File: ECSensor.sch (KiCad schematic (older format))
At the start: 4 parts

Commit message: Mostly complete Schematic
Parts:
- added Q?: Q_PMOS_DSG, symbol Device:Q_PMOS_DSG
- added R?: 150k, symbol Device:R_Small_US
- added R? (x2): 0, symbol Device:R_Small_US
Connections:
- net RE: now also R?.2
- net WE: now also R?.2
- new net: Q?.1 (D), R?.1
- new net: Q?.2 (S), R?.1
- new net: Q?.3 (G), R?.1
- new net AVDD: R?.2
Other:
- note added: "P-Channel FET used \nto short RE and WE\non power off"
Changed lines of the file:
@@
 $Descr A4 11693 8268
 encoding utf-8
-Sheet 2 2
+Sheet 3 3
 Title ""
 Date ""
@@
 U 1 1 5DF76279
 P 3350 3850
+AR Path="/5DF7340A/5DF76279" Ref="C?"  Part="1"
+AR Path="/5DF54D0C/5DF76279" Ref="C?"  Part="1"
 F 0 "C?" H 3442 3896 50  0000 L CNN
 F 1 "0.1u" H 3442 3805 50  0000 L CNN
@@
 U 1 1 5DF76497
 P 3000 3600
+AR Path="/5DF7340A/5DF76497" Ref="C?"  Part="1"
+AR Path="/5DF54D0C/5DF76497" Ref="C?"  Part="1"
 F 0 "C?" H 3092 3646 50  0000 L CNN
 F 1 "0.1u" H 3092 3555 50  0000 L CNN
@@
 U 1 1 5DF768A0
 P 3700 4100
+AR Path="/5DF7340A/5DF768A0" Ref="C?"  Part="1"
+AR Path="/5DF54D0C/5DF768A0" Ref="C?"  Part="1"
 F 0 "C?" H 3792 4146 50  0000 L CNN
 F 1 "0.1u" H 3792 4055 50  0000 L CNN
@@
 U 1 1 5DF7EEA4
 P 4100 3600
+AR Path="/5DF7340A/5DF7EEA4" Ref="J?"  Part="1"
+AR Path="/5DF54D0C/5DF7EEA4" Ref="J?"  Part="1"
 F 0 "J?" H 3974 3633 50  0000 R CNN
 F 1 "EC_Sensor_Input_3_Pin" H 3974 3542 50  0000 R CNN
@@
 Wire Wire Line
 	3450 3200 3450 3500
+$Comp
+L Device:Q_PMOS_DSG Q?
+U 1 1 5E0080C3
+P 1550 1350
+AR Path="/5DF54D0C/5E0080C3" Ref="Q?"  Part="1"
+AR Path="/5DF7340A/5E0080C3" Ref="Q?"  Part="1"
+F 0 "Q?" H 1755 1396 50  0000 L CNN
+F 1 "Q_PMOS_DSG" H 1755 1305 50  0000 L CNN
+F 2 "" H 1750 1450 50  0001 C CNN
+F 3 "~" H 1550 1350 50  0001 C CNN
+	1    1550 1350
+	1    0    0    -1
+$EndComp
+$Comp
+L Device:R_Small_US R?
+U 1 1 5E00BDC0
+P 1250 1350
+AR Path="/5DF54D0C/5E00BDC0" Ref="R?"  Part="1"
+AR Path="/5DF7340A/5E00BDC0" Ref="R?"  Part="1"
+F 0 "R?" V 1045 1350 50  0000 C CNN
+F 1 "150k" V 1136 1350 50  0000 C CNN
+F 2 "" H 1250 1350 50  0001 C CNN
+F 3 "~" H 1250 1350 50  0001 C CNN
+	1    1250 1350
+	0    1    1    0
+$EndComp
+$Comp
+L Device:R_Small_US R?
+U 1 1 5E00C4B8
+P 1650 1050
+AR Path="/5DF54D0C/5E00C4B8" Ref="R?"  Part="1"
+AR Path="/5DF7340A/5E00C4B8" Ref="R?"  Part="1"
+F 0 "R?" H 1582 1004 50  0000 R CNN
+F 1 "0" H 1582 1095 50  0000 R CNN
+F 2 "" H 1650 1050 50  0001 C CNN
+F 3 "~" H 1650 1050 50  0001 C CNN
+	1    1650 1050
+	-1   0    0    1
+$EndComp
+$Comp
+L Device:R_Small_US R?
+U 1 1 5E00C73E
+P 1650 1650
+AR Path="/5DF54D0C/5E00C73E" Ref="R?"  Part="1"
+AR Path="/5DF7340A/5E00C73E" Ref="R?"  Part="1"
+F 0 "R?" H 1718 1696 50  0000 L CNN
+F 1 "0" H 1718 1605 50  0000 L CNN
+F 2 "" H 1650 1650 50  0001 C CNN
+F 3 "~" H 1650 1650 50  0001 C CNN
+	1    1650 1650
+	1    0    0    -1
+$EndComp
+Text GLabel 1000 1350 0    50   Input ~ 0
+AVDD
+Wire Wire Line
+	1000 1350 1150 1350
+Text Label 3150 2900 2    50   ~ 0
+RE
+Text Label 3150 3050 2    50   ~ 0
+WE
+Text Label 3150 3200 2    50   ~ 0
+CE
+Text Label 1650 800  1    50   ~ 0
+RE
+Text Label 1650 1900 3    50   ~ 0
+WE
+Wire Wire Line
+	1650 1750 1650 1900
+Wire Wire Line
+	1650 950  1650 800
+Wire Notes Line style solid
+	2300 650  2300 2050
+Wire Notes Line style solid
+	2300 2050 700  2050
+Wire Notes Line style solid
+	700  2050 700  650
+Wire Notes Line style solid
+	700  650  2300 650
+Text Notes 750  2000 0    50   ~ 0
+P-Channel FET used \nto short RE and WE\non power off
 $EndSCHEMATC

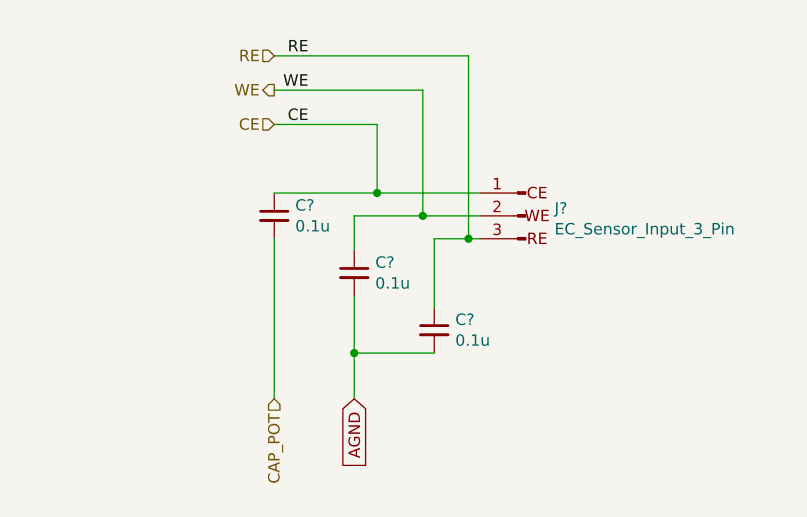
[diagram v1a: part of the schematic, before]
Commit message: Completed Power Supply Filtering
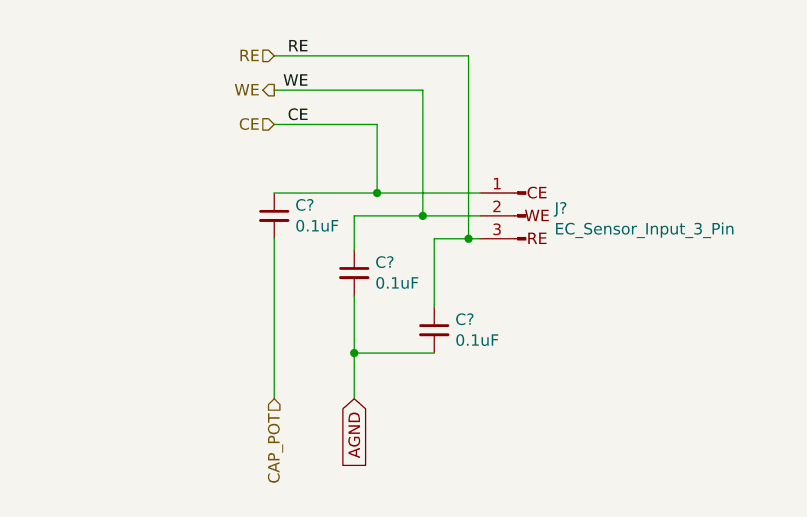
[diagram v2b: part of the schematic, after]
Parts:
- C? (x3): value 0.1u -> 0.1uF
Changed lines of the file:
@@
 AR Path="/5DF54D0C/5DF76279" Ref="C?"  Part="1"
 F 0 "C?" H 3442 3896 50  0000 L CNN
-F 1 "0.1u" H 3442 3805 50  0000 L CNN
+F 1 "0.1uF" H 3442 3805 50  0000 L CNN
 F 2 "" H 3350 3850 50  0001 C CNN
 F 3 "~" H 3350 3850 50  0001 C CNN
@@
 AR Path="/5DF54D0C/5DF76497" Ref="C?"  Part="1"
 F 0 "C?" H 3092 3646 50  0000 L CNN
-F 1 "0.1u" H 3092 3555 50  0000 L CNN
+F 1 "0.1uF" H 3092 3555 50  0000 L CNN
 F 2 "" H 3000 3600 50  0001 C CNN
 F 3 "~" H 3000 3600 50  0001 C CNN
@@
 AR Path="/5DF54D0C/5DF768A0" Ref="C?"  Part="1"
 F 0 "C?" H 3792 4146 50  0000 L CNN
-F 1 "0.1u" H 3792 4055 50  0000 L CNN
+F 1 "0.1uF" H 3792 4055 50  0000 L CNN
 F 2 "" H 3700 4100 50  0001 C CNN
 F 3 "~" H 3700 4100 50  0001 C CNN

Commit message: Working on power input
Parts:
- C37, C38, C39: renamed from C?; footprint (none) -> Capacitor_SMD:C_0603_1608Metric
- J4: renamed from J?; footprint (none) -> Connector_PinHeader_2.54mm:PinHeader_1x03_P2.54mm_Horizontal
- Q2: renamed from Q?; footprint (none) -> Package_TO_SOT_SMD:SOT-23
- R12, R13, R14: renamed from R?; footprint (none) -> Resistor_SMD:R_0603_1608Metric
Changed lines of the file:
@@
 AGND
 $Comp
-L Device:C_Small C?
+L Device:C_Small C38
 U 1 1 5DF76279
 P 3350 3850
-AR Path="/5DF7340A/5DF76279" Ref="C?"  Part="1"
-AR Path="/5DF54D0C/5DF76279" Ref="C?"  Part="1"
-F 0 "C?" H 3442 3896 50  0000 L CNN
+AR Path="/5DF7340A/5DF76279" Ref="C38"  Part="1"
+AR Path="/5DF54D0C/5DF76279" Ref="C41"  Part="1"
+F 0 "C41" H 3442 3896 50  0000 L CNN
 F 1 "0.1uF" H 3442 3805 50  0000 L CNN
-F 2 "" H 3350 3850 50  0001 C CNN
+F 2 "Capacitor_SMD:C_0603_1608Metric" H 3350 3850 50  0001 C CNN
 F 3 "~" H 3350 3850 50  0001 C CNN
 	1    3350 3850
@@
 $EndComp
 $Comp
-L Device:C_Small C?
+L Device:C_Small C37
 U 1 1 5DF76497
 P 3000 3600
-AR Path="/5DF7340A/5DF76497" Ref="C?"  Part="1"
-AR Path="/5DF54D0C/5DF76497" Ref="C?"  Part="1"
-F 0 "C?" H 3092 3646 50  0000 L CNN
+AR Path="/5DF7340A/5DF76497" Ref="C37"  Part="1"
+AR Path="/5DF54D0C/5DF76497" Ref="C40"  Part="1"
+F 0 "C40" H 3092 3646 50  0000 L CNN
 F 1 "0.1uF" H 3092 3555 50  0000 L CNN
-F 2 "" H 3000 3600 50  0001 C CNN
+F 2 "Capacitor_SMD:C_0603_1608Metric" H 3000 3600 50  0001 C CNN
 F 3 "~" H 3000 3600 50  0001 C CNN
 	1    3000 3600
@@
 $EndComp
 $Comp
-L Device:C_Small C?
+L Device:C_Small C39
 U 1 1 5DF768A0
 P 3700 4100
-AR Path="/5DF7340A/5DF768A0" Ref="C?"  Part="1"
-AR Path="/5DF54D0C/5DF768A0" Ref="C?"  Part="1"
-F 0 "C?" H 3792 4146 50  0000 L CNN
+AR Path="/5DF7340A/5DF768A0" Ref="C39"  Part="1"
+AR Path="/5DF54D0C/5DF768A0" Ref="C42"  Part="1"
+F 0 "C42" H 3792 4146 50  0000 L CNN
 F 1 "0.1uF" H 3792 4055 50  0000 L CNN
-F 2 "" H 3700 4100 50  0001 C CNN
+F 2 "Capacitor_SMD:C_0603_1608Metric" H 3700 4100 50  0001 C CNN
 F 3 "~" H 3700 4100 50  0001 C CNN
 	1    3700 4100
@@
 $EndComp
 $Comp
-L chemcrab:EC_Sensor_Input_3_Pin J?
+L chemcrab:EC_Sensor_Input_3_Pin J4
 U 1 1 5DF7EEA4
 P 4100 3600
-AR Path="/5DF7340A/5DF7EEA4" Ref="J?"  Part="1"
-AR Path="/5DF54D0C/5DF7EEA4" Ref="J?"  Part="1"
-F 0 "J?" H 3974 3633 50  0000 R CNN
+AR Path="/5DF7340A/5DF7EEA4" Ref="J4"  Part="1"
+AR Path="/5DF54D0C/5DF7EEA4" Ref="J5"  Part="1"
+F 0 "J5" H 3974 3633 50  0000 R CNN
 F 1 "EC_Sensor_Input_3_Pin" H 3974 3542 50  0000 R CNN
-F 2 "" H 4100 3600 50  0001 C CNN
+F 2 "Connector_PinHeader_2.54mm:PinHeader_1x03_P2.54mm_Horizontal" H 4100 3600 50  0001 C CNN
 F 3 "~" H 4100 3600 50  0001 C CNN
 	1    4100 3600
@@
 	3450 3200 3450 3500
 $Comp
-L Device:Q_PMOS_DSG Q?
+L Device:Q_PMOS_DSG Q2
 U 1 1 5E0080C3
 P 1550 1350
-AR Path="/5DF54D0C/5E0080C3" Ref="Q?"  Part="1"
-AR Path="/5DF7340A/5E0080C3" Ref="Q?"  Part="1"
-F 0 "Q?" H 1755 1396 50  0000 L CNN
+AR Path="/5DF54D0C/5E0080C3" Ref="Q2"  Part="1"
+AR Path="/5DF7340A/5E0080C3" Ref="Q1"  Part="1"
+F 0 "Q2" H 1755 1396 50  0000 L CNN
 F 1 "Q_PMOS_DSG" H 1755 1305 50  0000 L CNN
-F 2 "" H 1750 1450 50  0001 C CNN
+F 2 "Package_TO_SOT_SMD:SOT-23" H 1750 1450 50  0001 C CNN
 F 3 "~" H 1550 1350 50  0001 C CNN
 	1    1550 1350
@@
 $EndComp
 $Comp
-L Device:R_Small_US R?
+L Device:R_Small_US R12
 U 1 1 5E00BDC0
 P 1250 1350
-AR Path="/5DF54D0C/5E00BDC0" Ref="R?"  Part="1"
-AR Path="/5DF7340A/5E00BDC0" Ref="R?"  Part="1"
-F 0 "R?" V 1045 1350 50  0000 C CNN
+AR Path="/5DF54D0C/5E00BDC0" Ref="R12"  Part="1"
+AR Path="/5DF7340A/5E00BDC0" Ref="R9"  Part="1"
+F 0 "R12" V 1045 1350 50  0000 C CNN
 F 1 "150k" V 1136 1350 50  0000 C CNN
-F 2 "" H 1250 1350 50  0001 C CNN
+F 2 "Resistor_SMD:R_0603_1608Metric" H 1250 1350 50  0001 C CNN
 F 3 "~" H 1250 1350 50  0001 C CNN
 	1    1250 1350
@@
 $EndComp
 $Comp
-L Device:R_Small_US R?
+L Device:R_Small_US R13
 U 1 1 5E00C4B8
 P 1650 1050
-AR Path="/5DF54D0C/5E00C4B8" Ref="R?"  Part="1"
-AR Path="/5DF7340A/5E00C4B8" Ref="R?"  Part="1"
-F 0 "R?" H 1582 1004 50  0000 R CNN
+AR Path="/5DF54D0C/5E00C4B8" Ref="R13"  Part="1"
+AR Path="/5DF7340A/5E00C4B8" Ref="R10"  Part="1"
+F 0 "R13" H 1582 1004 50  0000 R CNN
 F 1 "0" H 1582 1095 50  0000 R CNN
-F 2 "" H 1650 1050 50  0001 C CNN
+F 2 "Resistor_SMD:R_0603_1608Metric" H 1650 1050 50  0001 C CNN
 F 3 "~" H 1650 1050 50  0001 C CNN
 	1    1650 1050
@@
 $EndComp
 $Comp
-L Device:R_Small_US R?
+L Device:R_Small_US R14
 U 1 1 5E00C73E
 P 1650 1650
-AR Path="/5DF54D0C/5E00C73E" Ref="R?"  Part="1"
-AR Path="/5DF7340A/5E00C73E" Ref="R?"  Part="1"
-F 0 "R?" H 1718 1696 50  0000 L CNN
+AR Path="/5DF54D0C/5E00C73E" Ref="R14"  Part="1"
+AR Path="/5DF7340A/5E00C73E" Ref="R11"  Part="1"
+F 0 "R14" H 1718 1696 50  0000 L CNN
 F 1 "0" H 1718 1605 50  0000 L CNN
-F 2 "" H 1650 1650 50  0001 C CNN
+F 2 "Resistor_SMD:R_0603_1608Metric" H 1650 1650 50  0001 C CNN
 F 3 "~" H 1650 1650 50  0001 C CNN
 	1    1650 1650

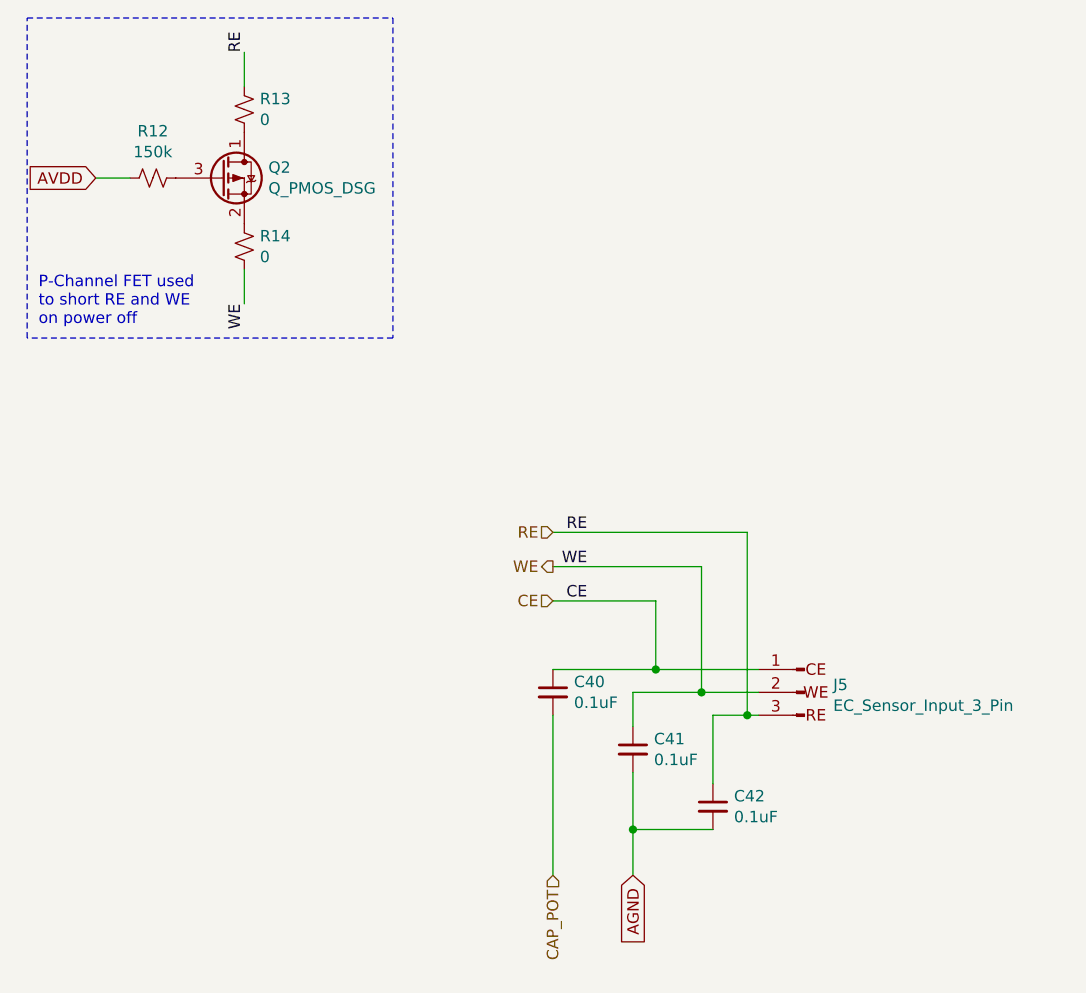
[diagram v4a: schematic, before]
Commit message: Removed unnecessary components
Move things like the Battery Charging circuitry to a separate sheet that can be readded in the future.
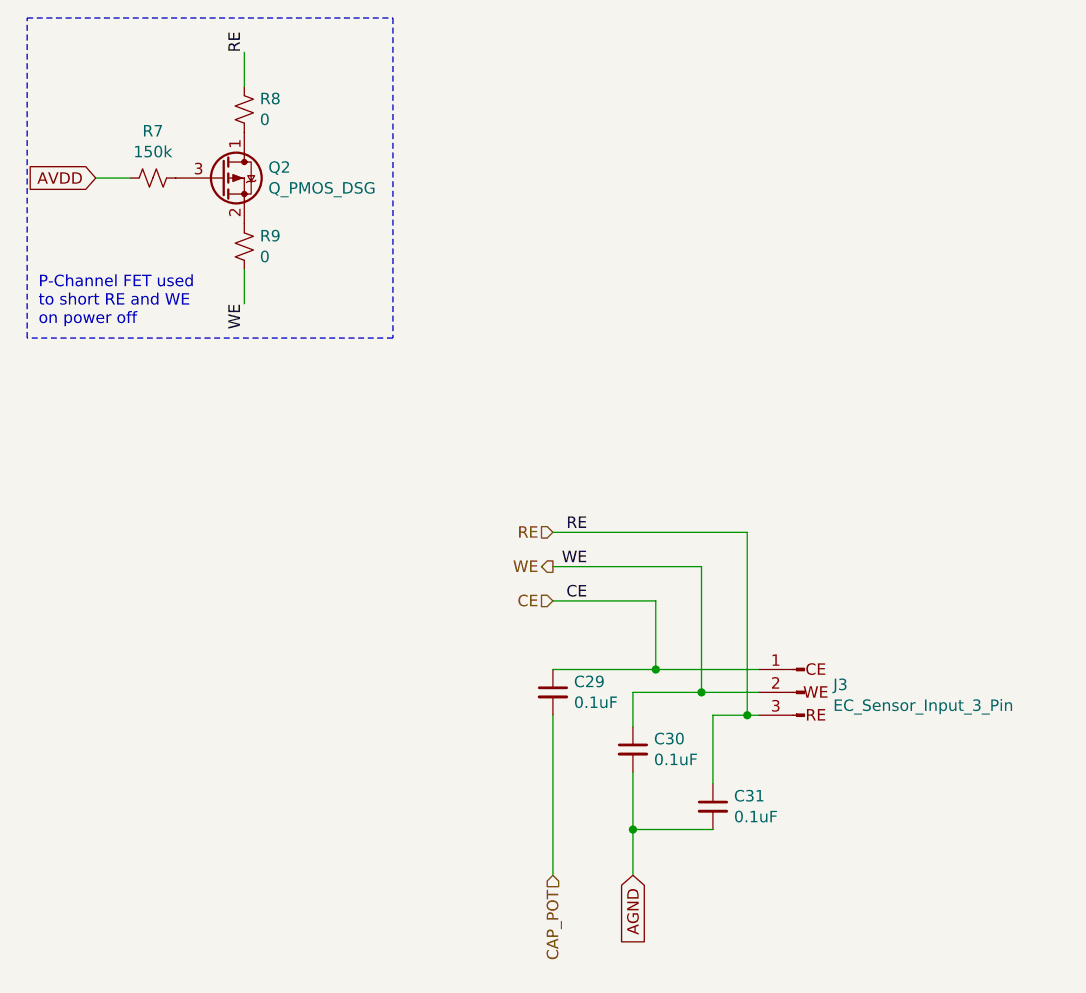
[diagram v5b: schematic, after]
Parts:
- renumbered C37 to C26, C38 to C27, C39 to C28, J4 to J2, R12 to R7, R13 to R8, R14 to R9
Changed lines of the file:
@@
 EESchema Schematic File Version 4
-LIBS:aducm_board-cache
 EELAYER 30 0
 EELAYER END
 $Descr A4 11693 8268
 encoding utf-8
-Sheet 3 4
+Sheet 3 3
 Title "ADuCM355 Template"
 Date ""
@@
 AGND
 $Comp
-L Device:C_Small C38
+L Device:C_Small C27
 U 1 1 5DF76279
 P 3350 3850
-AR Path="/5DF7340A/5DF76279" Ref="C38"  Part="1"
-AR Path="/5DF54D0C/5DF76279" Ref="C41"  Part="1"
-F 0 "C41" H 3442 3896 50  0000 L CNN
+AR Path="/5DF7340A/5DF76279" Ref="C27"  Part="1"
+AR Path="/5DF54D0C/5DF76279" Ref="C30"  Part="1"
+F 0 "C30" H 3442 3896 50  0000 L CNN
 F 1 "0.1uF" H 3442 3805 50  0000 L CNN
 F 2 "Capacitor_SMD:C_0603_1608Metric" H 3350 3850 50  0001 C CNN
@@
 $EndComp
 $Comp
-L Device:C_Small C37
+L Device:C_Small C26
 U 1 1 5DF76497
 P 3000 3600
-AR Path="/5DF7340A/5DF76497" Ref="C37"  Part="1"
-AR Path="/5DF54D0C/5DF76497" Ref="C40"  Part="1"
-F 0 "C40" H 3092 3646 50  0000 L CNN
+AR Path="/5DF7340A/5DF76497" Ref="C26"  Part="1"
+AR Path="/5DF54D0C/5DF76497" Ref="C29"  Part="1"
+F 0 "C29" H 3092 3646 50  0000 L CNN
 F 1 "0.1uF" H 3092 3555 50  0000 L CNN
 F 2 "Capacitor_SMD:C_0603_1608Metric" H 3000 3600 50  0001 C CNN
@@
 $EndComp
 $Comp
-L Device:C_Small C39
+L Device:C_Small C28
 U 1 1 5DF768A0
 P 3700 4100
-AR Path="/5DF7340A/5DF768A0" Ref="C39"  Part="1"
-AR Path="/5DF54D0C/5DF768A0" Ref="C42"  Part="1"
-F 0 "C42" H 3792 4146 50  0000 L CNN
+AR Path="/5DF7340A/5DF768A0" Ref="C28"  Part="1"
+AR Path="/5DF54D0C/5DF768A0" Ref="C31"  Part="1"
+F 0 "C31" H 3792 4146 50  0000 L CNN
 F 1 "0.1uF" H 3792 4055 50  0000 L CNN
 F 2 "Capacitor_SMD:C_0603_1608Metric" H 3700 4100 50  0001 C CNN
@@
 $EndComp
 $Comp
-L chemcrab:EC_Sensor_Input_3_Pin J4
+L chemcrab:EC_Sensor_Input_3_Pin J2
 U 1 1 5DF7EEA4
 P 4100 3600
-AR Path="/5DF7340A/5DF7EEA4" Ref="J4"  Part="1"
-AR Path="/5DF54D0C/5DF7EEA4" Ref="J5"  Part="1"
-F 0 "J5" H 3974 3633 50  0000 R CNN
+AR Path="/5DF7340A/5DF7EEA4" Ref="J2"  Part="1"
+AR Path="/5DF54D0C/5DF7EEA4" Ref="J3"  Part="1"
+F 0 "J3" H 3974 3633 50  0000 R CNN
 F 1 "EC_Sensor_Input_3_Pin" H 3974 3542 50  0000 R CNN
 F 2 "Connector_PinHeader_2.54mm:PinHeader_1x03_P2.54mm_Horizontal" H 4100 3600 50  0001 C CNN
@@
 $EndComp
 $Comp
-L Device:R_Small_US R12
+L Device:R_Small_US R7
 U 1 1 5E00BDC0
 P 1250 1350
-AR Path="/5DF54D0C/5E00BDC0" Ref="R12"  Part="1"
-AR Path="/5DF7340A/5E00BDC0" Ref="R9"  Part="1"
-F 0 "R12" V 1045 1350 50  0000 C CNN
+AR Path="/5DF54D0C/5E00BDC0" Ref="R7"  Part="1"
+AR Path="/5DF7340A/5E00BDC0" Ref="R4"  Part="1"
+F 0 "R7" V 1045 1350 50  0000 C CNN
 F 1 "150k" V 1136 1350 50  0000 C CNN
 F 2 "Resistor_SMD:R_0603_1608Metric" H 1250 1350 50  0001 C CNN
@@
 $EndComp
 $Comp
-L Device:R_Small_US R13
+L Device:R_Small_US R8
 U 1 1 5E00C4B8
 P 1650 1050
-AR Path="/5DF54D0C/5E00C4B8" Ref="R13"  Part="1"
-AR Path="/5DF7340A/5E00C4B8" Ref="R10"  Part="1"
-F 0 "R13" H 1582 1004 50  0000 R CNN
+AR Path="/5DF54D0C/5E00C4B8" Ref="R8"  Part="1"
+AR Path="/5DF7340A/5E00C4B8" Ref="R5"  Part="1"
+F 0 "R8" H 1582 1004 50  0000 R CNN
 F 1 "0" H 1582 1095 50  0000 R CNN
 F 2 "Resistor_SMD:R_0603_1608Metric" H 1650 1050 50  0001 C CNN
@@
 $EndComp
 $Comp
-L Device:R_Small_US R14
+L Device:R_Small_US R9
 U 1 1 5E00C73E
 P 1650 1650
-AR Path="/5DF54D0C/5E00C73E" Ref="R14"  Part="1"
-AR Path="/5DF7340A/5E00C73E" Ref="R11"  Part="1"
-F 0 "R14" H 1718 1696 50  0000 L CNN
+AR Path="/5DF54D0C/5E00C73E" Ref="R9"  Part="1"
+AR Path="/5DF7340A/5E00C73E" Ref="R6"  Part="1"
+F 0 "R9" H 1718 1696 50  0000 L CNN
 F 1 "0" H 1718 1605 50  0000 L CNN
 F 2 "Resistor_SMD:R_0603_1608Metric" H 1650 1650 50  0001 C CNN

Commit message: cleaning
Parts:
- J2: symbol chemcrab:EC_Sensor_Input_3_Pin -> SIB_Footprint:EC_Sensor_Input_3_Pin
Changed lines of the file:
@@
 EESchema Schematic File Version 4
+LIBS:aducm_board-cache
 EELAYER 30 0
 EELAYER END
@@
 $EndComp
 $Comp
-L chemcrab:EC_Sensor_Input_3_Pin J2
+L SIB_Footprint:EC_Sensor_Input_3_Pin J2
 U 1 1 5DF7EEA4
 P 4100 3600
